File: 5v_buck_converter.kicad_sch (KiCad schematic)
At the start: 8 parts, among them U3 TPS562231DRLR

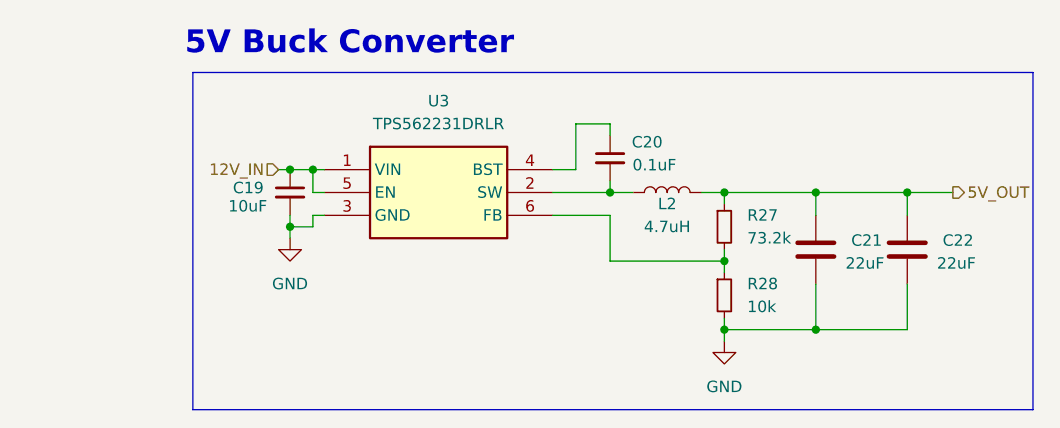
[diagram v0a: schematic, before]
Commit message: redid cypd layout, halfway through 12v buck layout
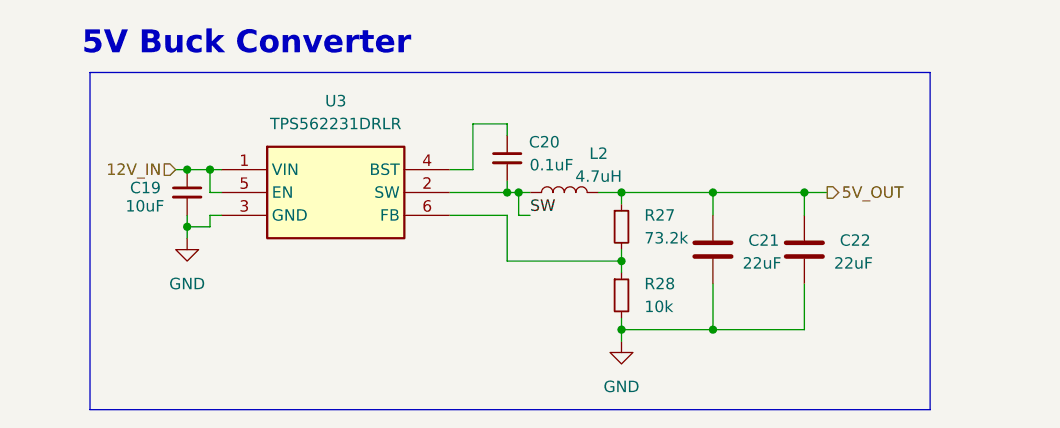
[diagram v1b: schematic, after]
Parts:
- L2: footprint UTSVT_Passive:INDPM110100X400N -> UTSVT_Passive:INDPM5452X300N; Manufacturer_Name Bourns -> Kyocera; Mouser Part Number SRP1038CC-R47M -> LMLP0506M4R7DTAS
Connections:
- net SW: now reaches C20.2, L2.1, U3.2 (SW)
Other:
- moved on the sheet: C19, C20, C21, C22, L2, R27, R28, U3

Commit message: big component layout moment
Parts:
- added TP15: 5V_SET, TestPoint:TestPoint_THTPad_1.0x1.0mm_Drill0.5mm, symbol Connector:TestPoint
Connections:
- net at R27.2, R28.1, U3.6 (FB): now also TP15.1
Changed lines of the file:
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@@
+	)
+	(junction
+		(at 153.67 105.41)
+		(diameter 0)
+		(color 0 0 0 0)
 	)
 	(junction
@@
 	(wire
 		(pts
+			(xy 153.67 105.41) (xy 160.02 105.41)
+		)
+		(stroke
+			(width 0)
+			(type default)
+		)
+	)
+	(wire
+		(pts
 			(xy 143.51 95.25) (xy 143.51 90.17)
 		)
@@
 	(wire
 		(pts
-			(xy 147.32 105.41) (xy 160.02 105.41)
+			(xy 147.32 105.41) (xy 153.67 105.41)
 		)
 		(stroke
@@
 	(wire
 		(pts
+			(xy 151.13 111.76) (xy 151.13 113.03)
+		)
+		(stroke
+			(width 0)
+			(type default)
+		)
+	)
+	(wire
+		(pts
 			(xy 180.34 107.95) (xy 180.34 113.03)
 		)
@@
 	(wire
 		(pts
+			(xy 151.13 113.03) (xy 153.67 113.03)
+		)
+		(stroke
+			(width 0)
+			(type default)
+		)
+	)
+	(wire
+		(pts
 			(xy 111.76 101.6) (xy 111.76 102.87)
 		)
@@
 		(pts
 			(xy 160.02 106.68) (xy 160.02 105.41)
+		)
+		(stroke
+			(width 0)
+			(type default)
+		)
+	)
+	(wire
+		(pts
+			(xy 153.67 105.41) (xy 153.67 113.03)
 		)
 		(stroke
@@
 					(unit 1)
 				)
+			)
+		)
+	)
+	(symbol
+		(lib_id "Connector:TestPoint")
+		(at 151.13 111.76 0)
+		(mirror y)
+		(unit 1)
+		(exclude_from_sim no)
+		(in_bom yes)
+		(on_board yes)
+		(dnp no)
+		(property "Reference" "TP15"
+			(at 148.59 107.1879 0)
+			(effects
+				(font
+					(size 1.27 1.27)
+				)
+				(justify left)
+			)
+		)
+		(property "Value" "5V_SET"
+			(at 148.59 109.7279 0)
+			(effects
+				(font
+					(size 1.27 1.27)
+				)
+				(justify left)
+			)
+		)
+		(property "Footprint" "TestPoint:TestPoint_THTPad_1.0x1.0mm_Drill0.5mm"
+			(at 146.05 111.76 0)
+			(effects
+				(font
+					(size 1.27 1.27)
+				)
+				(hide yes)
+			)
+		)
+		(property "Datasheet" "~"
+			(at 146.05 111.76 0)
+			(effects
+				(font
+					(size 1.27 1.27)
+				)
+				(hide yes)
+			)
+		)
+		(property "Description" "test point"
+			(at 151.13 111.76 0)
+			(effects
+				(font
+					(size 1.27 1.27)
+				)
+				(hide yes)
+			)
+		)
+		(pin "1"
+		)
+		(instances
+			(project "USBCPowerPCB"
+				(path "/f58400c5-df4b-4929-8d2b-33c0fe23fcd9/4f21da9f-d1d7-4b66-a00f-51f47ae1c74b"
+					(reference "TP15")
+					(unit 1)
+				)

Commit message: addressed some review comments from my 🐐 champers fu
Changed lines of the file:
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@@
-	)
-	(junction
-		(at 148.59 97.79)
-		(diameter 0)
-		(color 0 0 0 0)
 	)
 	(junction
@@
 	(wire
 		(pts
-			(xy 147.32 100.33) (xy 147.32 105.41)
+			(xy 143.51 100.33) (xy 143.51 105.41)
 		)
 		(stroke
@@
 	(wire
 		(pts
-			(xy 147.32 105.41) (xy 153.67 105.41)
+			(xy 143.51 105.41) (xy 153.67 105.41)
 		)
 		(stroke
@@
 	(wire
 		(pts
-			(xy 148.59 100.33) (xy 148.59 97.79)
+			(xy 147.32 100.33) (xy 147.32 97.79)
 		)
 		(stroke
@@
 	(wire
 		(pts
-			(xy 140.97 100.33) (xy 147.32 100.33)
+			(xy 140.97 100.33) (xy 143.51 100.33)
 		)
 		(stroke
@@
 	(wire
 		(pts
-			(xy 147.32 97.79) (xy 148.59 97.79)
+			(xy 147.32 97.79) (xy 149.86 97.79)
 		)
 		(stroke
@@
 	(wire
 		(pts
-			(xy 148.59 97.79) (xy 149.86 97.79)
-		)
-		(stroke
-			(width 0)
-			(type default)
-		)
-	)
-	(wire
-		(pts
 			(xy 147.32 96.52) (xy 147.32 97.79)
 		)
@@
 	(wire
 		(pts
-			(xy 148.59 100.33) (xy 149.86 100.33)
+			(xy 147.32 100.33) (xy 148.59 100.33)
 		)
 		(stroke
@@
 	)
 	(label "SW"
-		(at 149.86 100.33 0)
+		(at 148.59 100.33 0)
 		(fields_autoplaced yes)
 		(effects

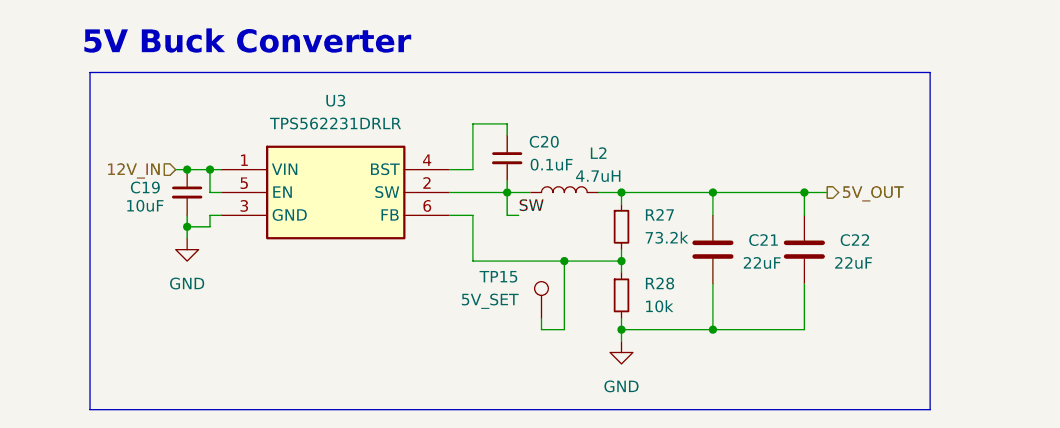
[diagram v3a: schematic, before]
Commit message: added fuse to protect 5V buck converter output
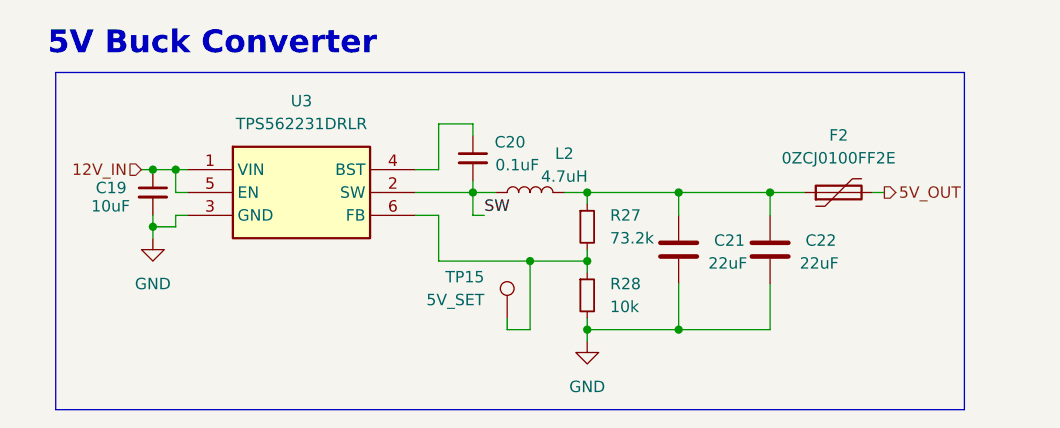
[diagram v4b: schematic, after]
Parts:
- added F2: 0ZCJ0100FF2E, Fuse:Fuse_1206_3216Metric, symbol Device:Polyfuse
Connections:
- net 5V_OUT: now also F2.2; no longer C21.1, C22.1, L2.2, R27.1
- new net: C21.1, C22.1, F2.1, L2.2, R27.1
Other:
- moved on the sheet: C19, C20, C21, C22, L2, R27, R28, TP15, U3

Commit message: i am jesus christ in the flesh.
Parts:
- C19: Mouser Part Number GRM21BR61H106KE43L -> (none); P/N (none) -> GRM21BR61H106KE43L
- C20: Mouser Part Number C0805C104M5RACTU -> (none); P/N (none) -> C0805C104M5RACTU
- C21, C22: Mouser Part Number C2012X5R1V226M125AC -> (none); P/N (none) -> C2012X5R1V226M125AC
- F2: Mouser Part Number 0ZCJ0100FF2E -> (none); P/N (none) -> 0ZCJ0100FF2E
- L2: Mouser Part Number LMLP0506M4R7DTAS -> (none); P/N (none) -> LMLP0506M4R7DTAS
- R27: Mouser Part Number CRCW080573K2FKEA -> (none); P/N (none) -> CRCW080573K2FKEA
- R28: Mouser Part Number CRCW080510K0FKEAC -> (none); P/N (none) -> CRCW080510K0FKEAC
- U3: Mouser Part Number 595-TPS562231DRLR -> (none)
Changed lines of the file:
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@@
 			)
 		)
-		(property "Mouser Part Number" " GRM21BR61H106KE43L "
+		(property "Mouser Part Number" ""
 			(at 107.95 97.79 0)
 			(effects
@@
 		)
 		(property "SnapEDA_Link" ""
+			(at 107.95 97.79 0)
+			(effects
+				(font
+					(size 1.27 1.27)
+				)
+				(hide yes)
+			)
+		)
+		(property "P/N" " GRM21BR61H106KE43L "
 			(at 107.95 97.79 0)
 			(effects
@@
 			)
 		)
-		(property "Mouser Part Number" "C2012X5R1V226M125AC"
+		(property "Mouser Part Number" ""
 			(at 166.37 104.14 0)
 			(effects
@@
 		)
 		(property "SnapEDA_Link" ""
+			(at 166.37 104.14 0)
+			(effects
+				(font
+					(size 1.27 1.27)
+				)
+				(hide yes)
+			)
+		)
+		(property "P/N" "C2012X5R1V226M125AC"
 			(at 166.37 104.14 0)
 			(effects
@@
 			)
 		)
-		(property "Mouser Part Number" "C0805C104M5RACTU"
+		(property "Mouser Part Number" ""
 			(at 143.51 93.98 0)
 			(effects
@@
 		)
 		(property "SnapEDA_Link" ""
+			(at 143.51 93.98 0)
+			(effects
+				(font
+					(size 1.27 1.27)
+				)
+				(hide yes)
+			)
+		)
+		(property "P/N" "C0805C104M5RACTU"
 			(at 143.51 93.98 0)
 			(effects
@@
 			)
 		)
-		(property "Mouser Part Number" "C2012X5R1V226M125AC"
+		(property "Mouser Part Number" ""
 			(at 176.53 104.14 0)
 			(effects
@@
 		)
 		(property "SnapEDA_Link" ""
+			(at 176.53 104.14 0)
+			(effects
+				(font
+					(size 1.27 1.27)
+				)
+				(hide yes)
+			)
+		)
+		(property "P/N" "C2012X5R1V226M125AC"
 			(at 176.53 104.14 0)
 			(effects
@@
 			)
 		)
-		(property "Mouser Part Number" "CRCW080573K2FKEA"
+		(property "Mouser Part Number" ""
 			(at 156.21 101.6 0)
 			(effects
@@
 		)
 		(property "SnapEDA_Link" ""
+			(at 156.21 101.6 0)
+			(effects
+				(font
+					(size 1.27 1.27)
+				)
+				(hide yes)
+			)
+		)
+		(property "P/N" "CRCW080573K2FKEA"
 			(at 156.21 101.6 0)
 			(effects
@@
 			)
 		)
-		(property "Mouser Part Number" "CRCW080510K0FKEAC "
+		(property "Mouser Part Number" ""
 			(at 156.21 109.22 0)
 			(effects
@@
 		)
 		(property "SnapEDA_Link" ""
+			(at 156.21 109.22 0)
+			(effects
+				(font
+					(size 1.27 1.27)
+				)
+				(hide yes)
+			)
+		)
+		(property "P/N" "CRCW080510K0FKEAC"
 			(at 156.21 109.22 0)
 			(effects
@@
 			)
 		)
-		(property "Mouser Part Number" "0ZCJ0100FF2E"
+		(property "Mouser Part Number" ""
+			(at 184.15 97.79 0)
+			(effects
+				(font
+					(size 1.27 1.27)
+				)
+				(hide yes)
+			)
+		)
+		(property "P/N" "0ZCJ0100FF2E"
 			(at 184.15 97.79 0)
 			(effects
@@
 			)
 		)
-		(property "Mouser Part Number" "595-TPS562231DRLR"
+		(property "Mouser Part Number" ""
 			(at 123.19 90.17 0)
 			(effects
@@
 			)
 		)
-		(property "Mouser Part Number" "LMLP0506M4R7DTAS "
+		(property "Mouser Part Number" ""
 			(at 149.86 97.79 0)
 			(effects
@@
 			(at 149.86 97.79 0)
 			(effects
+				(font
+					(size 1.27 1.27)
+				)
+				(hide yes)
+			)
+		)
+		(property "P/N" "LMLP0506M4R7DTAS "
+			(at 149.86 97.79 0)
+			(effects
